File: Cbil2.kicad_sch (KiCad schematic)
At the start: 26 parts, among them J1 Conn_01x07_Male, U1 430152070826, U2 STM32G030K6T6, U3 HIH7130-000-001, U4 TC72-3.3MUA, U5 KP466PXTMA1, U6 KB_DELPS2.DI-THVG-2J8L-Z555, Y1 ABS07-32.768KHZ-6-4-T

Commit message: PCB layout
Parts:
- removed U2: STM32G030K6T6, symbol sigbo:STM32G030K6T6
- added C12, C13: 10u, Capacitor_SMD:C_0603_1608Metric, symbol Device:C
- added C14, C15: 0.05u, Capacitor_SMD:C_0603_1608Metric, symbol Device:C
- added LS1: Speaker, Buzzer_Beeper:Speaker_CUI_CMR-1206S-67, symbol Device:Speaker
- added R2: 10, Resistor_SMD:R_0603_1608Metric, symbol Device:R
- added U7: LM386, Cbil2-lib:SOIC127P600X175-8N, symbol Amplifier_Audio:LM386
- added U8: STM32G0B1KETxN, Package_QFP:LQFP-32_7x7mm_P0.8mm, symbol MCU_ST_STM32G0:STM32G0B1KETxN
- added VR1: PVG5A103C03R00, Cbil2-lib:PVG5A100C03R00, symbol Device:PVG5A103C03R00
- U1: footprint Whymote:430152070826 -> Cbil2-lib:430152070826
- U2: renamed from U?; footprint (none) -> Cbil2-lib:SOTFL95P240X88-3N
- U3: footprint (none) -> Cbil2-lib:HIH7130-000-001
- U4: footprint (none) -> Cbil2-lib:SOP65P490X110-8N
- U5: footprint (none) -> Cbil2-lib:KP466PXTMA1
- U6: footprint Whymote:KBDELPS2DITHVG2J8LZ555 -> Cbil2-lib:KBDELPS2DITHVG2J8LZ555
- U9: renamed from ?; footprint (none) -> Cbil2-lib:SOTFL95P240X88-3N
- Y1: footprint Whymote:ABS07 -> Cbil2-lib:ABS07
- gave numbers to parts that had none: 4
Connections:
- net VDD_3V3 is gone; now on net VDD: U1.1 (COM_1), U1.3 (COM_2)
- net ADC_1: now also U8.16 (PB1)
- net ADC_2: now also U8.15 (PB0)
- net GND: now also LS1.2, R2.2, U7.2 (-), U7.4 (GND), U8.5 (VSS), VR1.3 (CW)
- net NRST: now also U8.6 (PF2)
- net OSC_32_1: now also U8.2 (PC14)
- net OSC_32_2: now also U8.3 (PC15)
- net SPI_MISO: now also U8.10 (PA3)
- net SPI_MOSI: now also U8.11 (PA4)
- net SPI_NCK: now also U8.7 (PA0)
- net SPI_NSS: now also U8.18 (PA8)
- net VDD: now also U8.4 (VDD)
- net 5V: now reaches J1.1 (Pin_1)
- net 5V: now also U7.6 (V+)
- net SWDIO: now reaches J1.2 (Pin_2)
- net SWDIO: now also U8.24 (PA13)
- net SWCLK: now reaches J1.3 (Pin_3)
- net SWCLK: now also U8.25 (PA14)
- new net: C14.1, C15.1, U7.5
- new net: C14.2, R2.1
- new net: C13.2, VR1.1 (CCW)
- new net: C15.2, LS1.1
- new net: U7.3 (+), VR1.2 (WIPER)
- new net: C12.1, U7.8 (GAIN)
- new net: C12.2, U7.1 (GAIN)
- new net DAC_OUT: C13.1, U8.12 (PA5)
- no-connect marks 3 -> 20
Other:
- moved on the sheet: J1

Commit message: Add a few doodads
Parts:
- added R3, R4, R5, R6: 330, Capacitor_SMD:C_0603_1608Metric, symbol Device:R
- added U10: KB_DELPS2.DI-THVG-2J8L-Z555, Cbil2-lib:KBDELPS2DITHVG2J8LZ555, symbol Whymote:KB_DELPS2.DI-THVG-2J8L-Z555
- added U11, U12: KO DELPS1.22-UGVI-24-H3Q4, Cbil2-lib:KBDELPS2DITHVG2J8LZ555, symbol Whymote:KB_DELPS2.DI-THVG-2J8L-Z555
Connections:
- net 5V: now also U12.2 (A)
- net GND: now also U1.1 (COM_1), U1.3 (COM_2), R4.2, R5.2, R6.2
- net NRST: now also J1.4 (Pin_4)
- net VDD: now also R3.2, U11.2 (A); no longer U1.1 (COM_1), U1.3 (COM_2), U6.2 (A)
- net USART_TX: now reaches U8.19 (PA9/UCPD1_DBCC1)
- net USART_TX: now also J1.5 (Pin_5)
- net LED: now reaches U8.22 (PA11/PA9)
- net LED: now also U10.2 (A)
- new net: R6.1, U12.1 (K)
- new net: R5.1, U11.1 (K)
- new net: R4.1, U10.1 (K)
- new net: R3.1, U6.2 (A)
- no-connect marks 20 -> 18
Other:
- moved on the sheet: U6

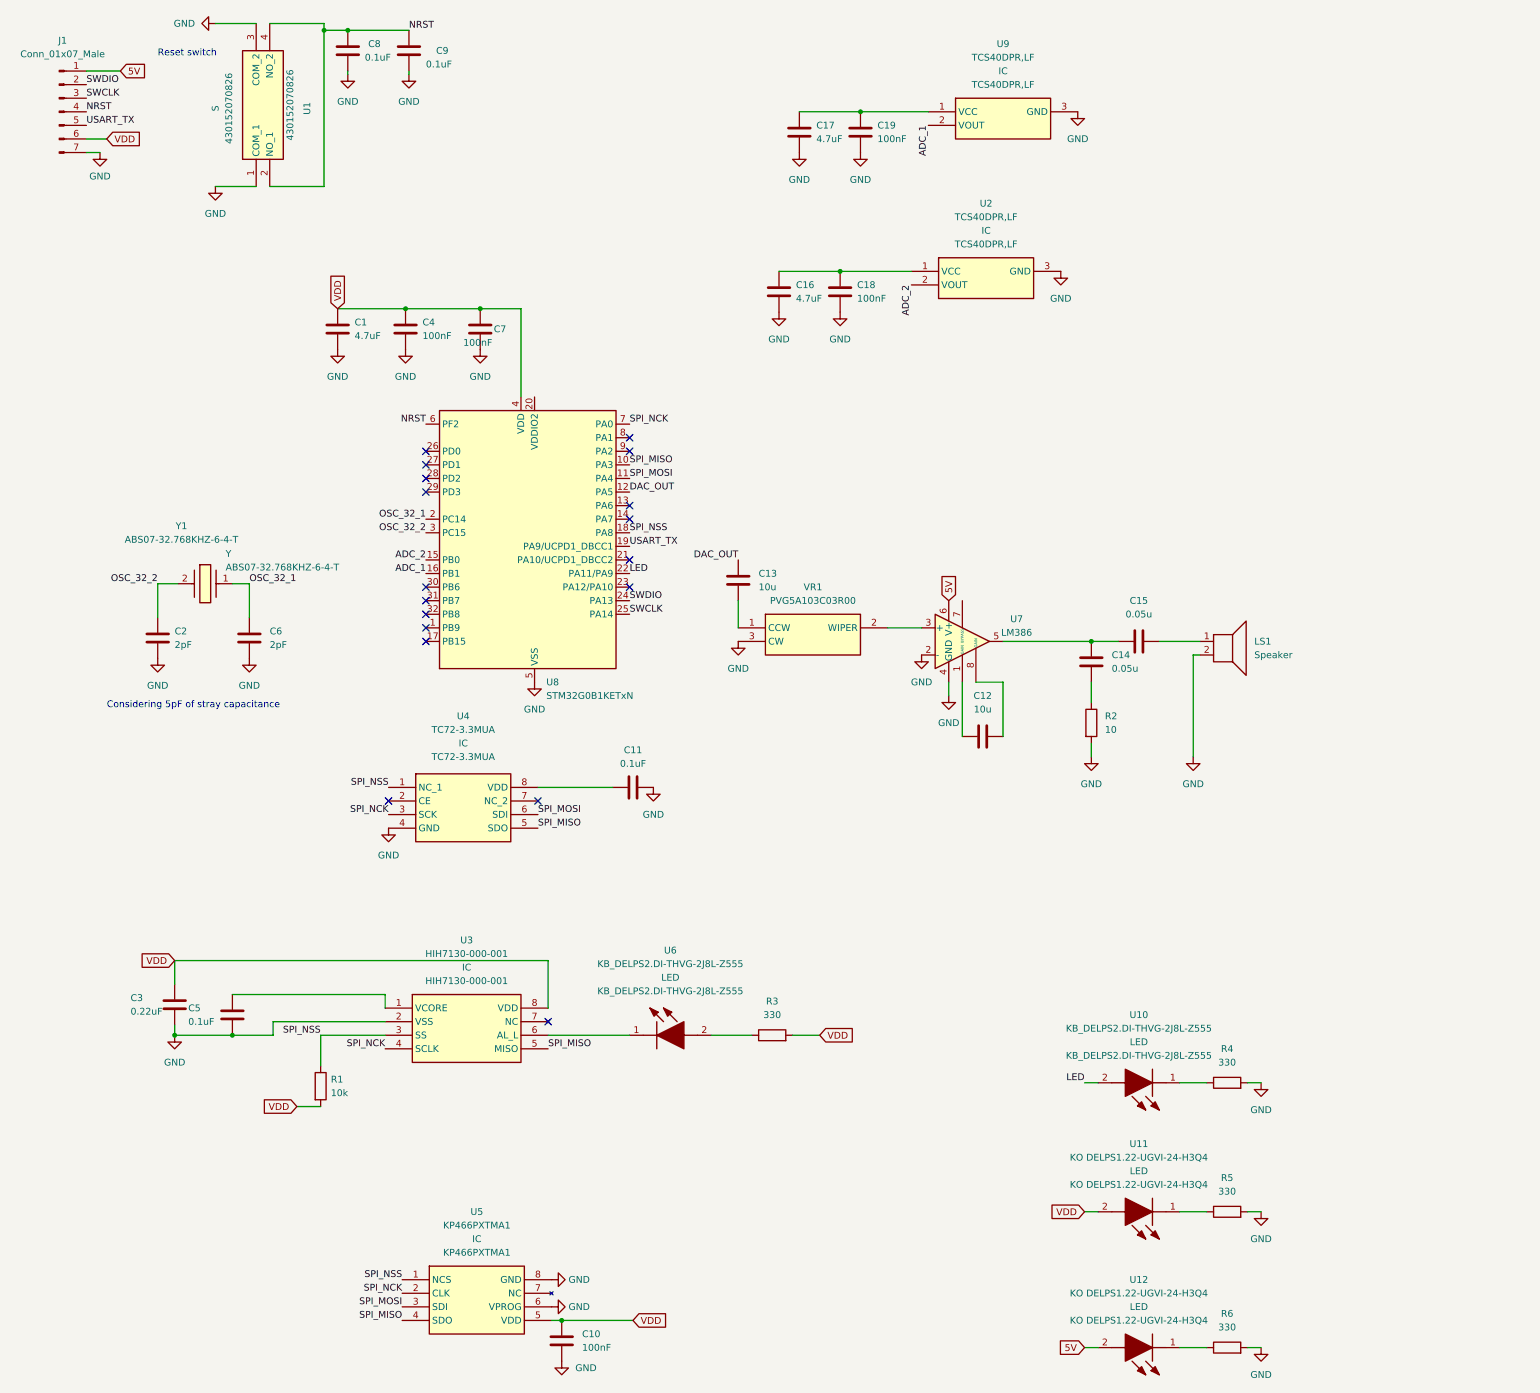
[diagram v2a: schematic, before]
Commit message: Add a screen
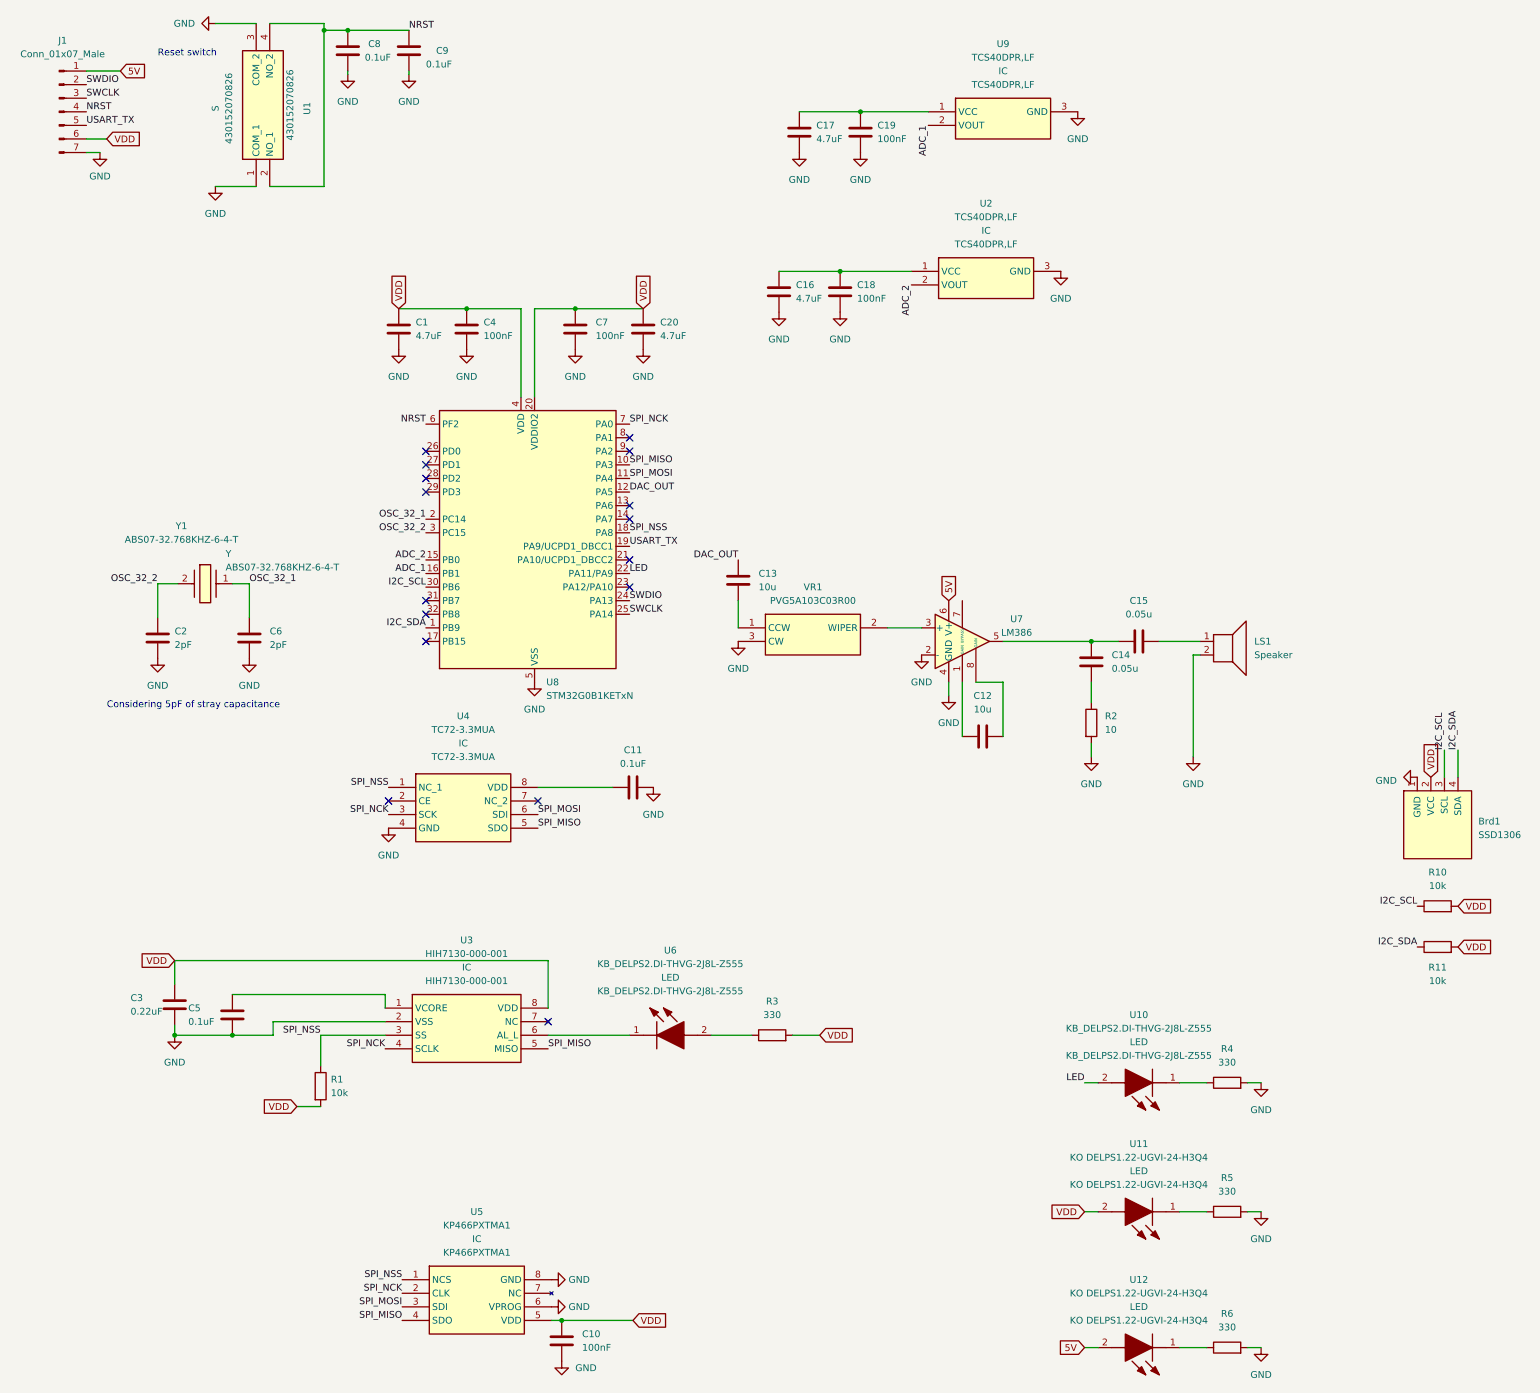
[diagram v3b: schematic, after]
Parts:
- added Brd1: SSD1306, SSD1306:128x64OLED, symbol SSD1306-128x64_OLED:SSD1306
- added C20: 4.7uF, Capacitor_SMD:C_0603_1608Metric, symbol Device:C
- added R10, R11: 10k, Resistor_SMD:R_0603_1608Metric_Pad0.98x0.95mm_HandSolder, symbol Device:R
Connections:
- net GND: now also Brd1.1 (GND), C20.2
- net VDD: now also U8.20 (VDDIO2), Brd1.2 (VCC), C20.1, R10.2, R11.2
- net I2C_SDA: now reaches U8.1 (PB9)
- net I2C_SDA: now also Brd1.4 (SDA), R11.1
- net I2C_SCL: now reaches U8.30 (PB6)
- net I2C_SCL: now also Brd1.3 (SCL), R10.1
- no-connect marks 18 -> 16

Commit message: Update layout
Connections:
- net LED: now also U8.29 (PD3); no longer U8.22 (PA11/PA9)
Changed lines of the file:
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@@
   (no_connect (at 128.27 121.92))
   (no_connect (at 90.17 101.6))
-  (no_connect (at 90.17 104.14))
   (no_connect (at 128.27 106.68))
   (no_connect (at 113.03 203.2))
+  (no_connect (at 128.27 119.38))
   (no_connect (at 111.125 161.925))
   (no_connect (at 83.185 161.925))
@@
     (effects (font (size 1.27 1.27)) (justify left bottom))
   )
-  (label "LED" (at 128.27 119.38 0) (fields_autoplaced)
-    (effects (font (size 1.27 1.27)) (justify left bottom))
-  )
   (label "OSC_32_1" (at 90.17 109.22 180) (fields_autoplaced)
     (effects (font (size 1.27 1.27)) (justify right bottom))
@@
     (effects (font (size 1.27 1.27)) (justify left bottom))
   )
+  (label "LED" (at 90.17 104.14 180) (fields_autoplaced)
+    (effects (font (size 1.27 1.27)) (justify right bottom))
+  )
   (label "LED" (at 213.36 214.63 180) (fields_autoplaced)
